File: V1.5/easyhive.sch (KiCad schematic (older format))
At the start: 105 parts, among them IC1 ATSAMD21G, IC2 BQ2407X, IC3 ADS1232, IC4 DS18B20U, IC5 XC6220B331, IC6 SARA-N310, IC7 TPS22919, J1 U.FL, J2 U.FL(2), K1 693043020611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

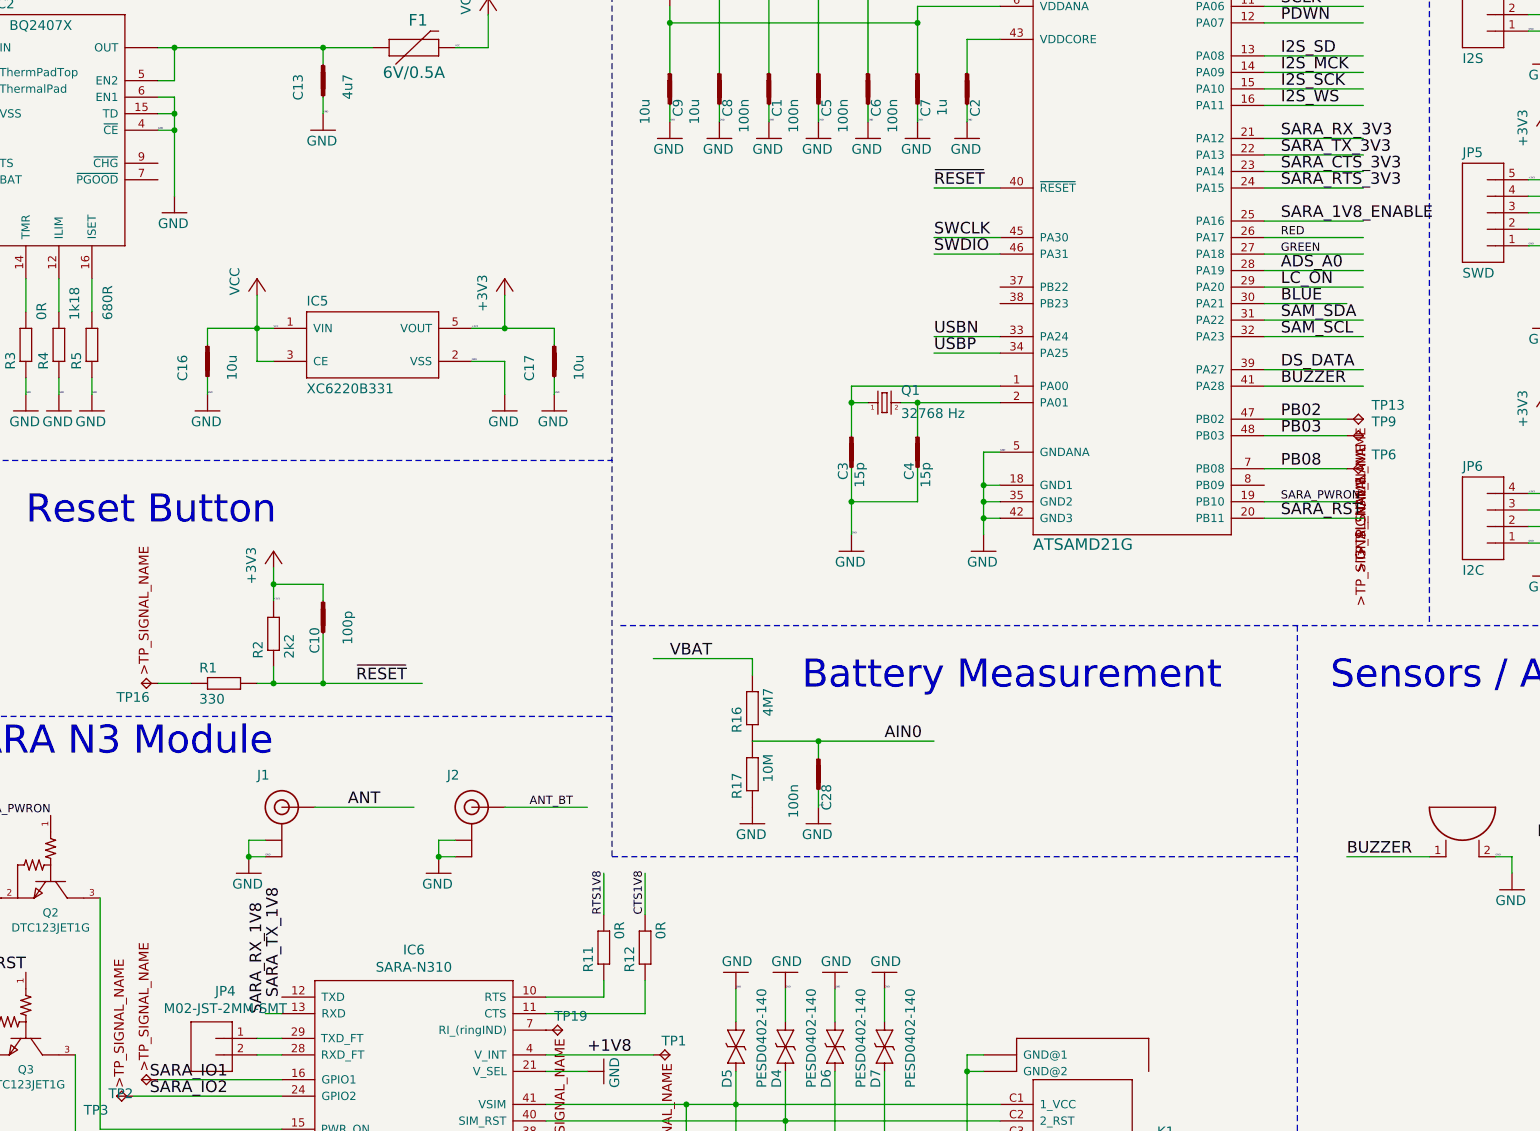
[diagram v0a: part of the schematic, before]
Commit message: Hardware optimization after Prototyp
- PA12: TX 3V3
- PA13: RX 3V3
- PA14: RTS 3V3
- PA15: CTS 3V3
- insert 2x R0 between TX/RX track
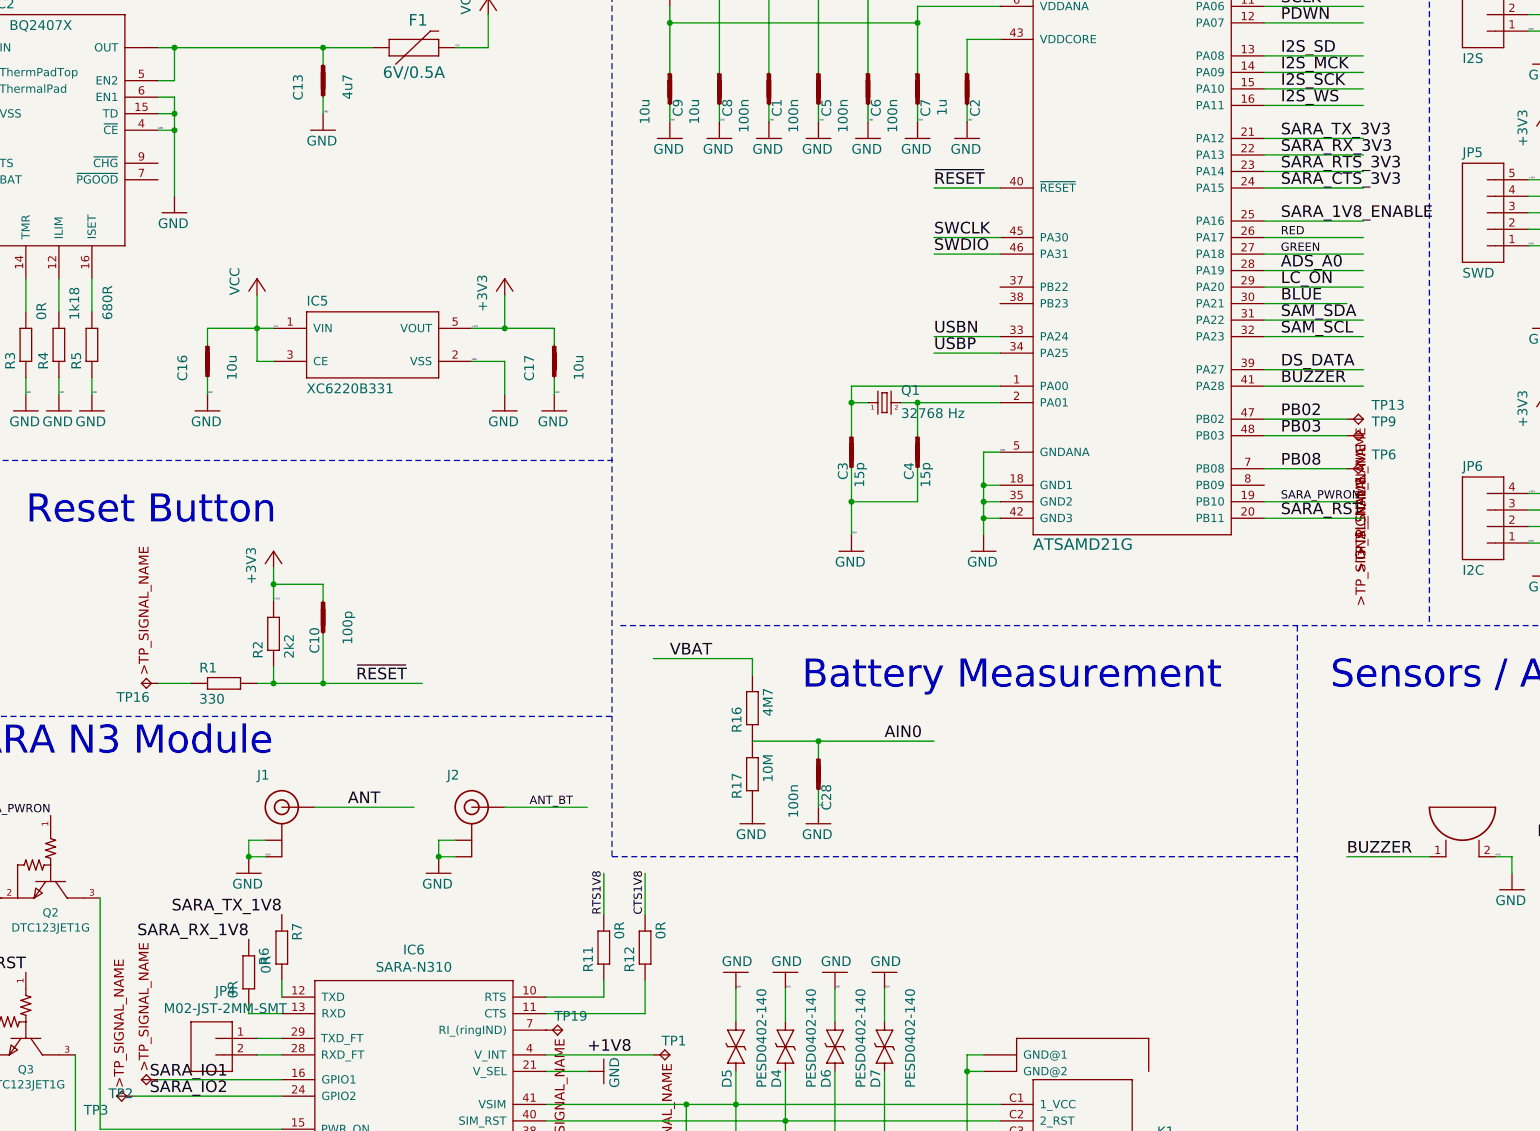
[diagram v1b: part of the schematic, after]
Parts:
- added R6, R7: 0R, easyhive:C0402, symbol easyhive:RESISTOR-0402
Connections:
- wire segments 412 -> 414
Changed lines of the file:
@@
 Text Label 12900 2250 0    70   ~ 0
 I2S_SD
-Text Label 12900 2950 0    70   ~ 0
-SARA_CTS_3V3
 Text Label 12900 3250 0    70   ~ 0
 SARA_1V8_ENABLE
-Text Label 12900 3050 0    70   ~ 0
-SARA_RTS_3V3
 Text Label 14900 7000 2    70   ~ 0
 DS_DATA
@@
 Text Label 8700 9200 0    70   ~ 0
 ANT_DET
-Text Label 6850 7950 1    70   ~ 0
-SARA_TX_1V8
-Text Label 12900 2750 0    70   ~ 0
-SARA_RX_3V3
-Text Label 6750 8050 1    70   ~ 0
-SARA_RX_1V8
-Text Label 12900 2850 0    70   ~ 0
-SARA_TX_3V3
 Text Label 6150 9650 0    70   ~ 0
 SARA_SDA
@@
 $EndComp
 $Comp
-L easyhive:MBR0520LT D1
-U 1 1 8D141E84
-P 3600 2200
-F 0 "D1" H 3700 2219 59  0000 L BNN
-F 1 "MBR0520LT" H 3700 2109 59  0000 L BNN
-F 2 "easyhive:SOD123" H 3600 2200 50  0001 C CNN
-F 3 "" H 3600 2200 50  0001 C CNN
-F 4 "auch anderer Hersteller moeglich" H 3600 2200 50  0001 C CNN "Description"
-F 5 "MBR0520LT" H 3600 2200 50  0001 C CNN "MPN"
-F 6 "ON Semiconductor" H 3600 2200 50  0001 C CNN "Manufacturer"
-	1    3600 2200
-	1    0    0    -1
-$EndComp
-$Comp
-L easyhive:MBR0520LT D2
-U 1 1 20478EC3
-P 3600 2900
-F 0 "D2" H 3700 2919 59  0000 L BNN
-F 1 "MBR0520LT" H 3700 2809 59  0000 L BNN
-F 2 "easyhive:SOD123" H 3600 2900 50  0001 C CNN
-F 3 "" H 3600 2900 50  0001 C CNN
-F 4 "auch anderer Hersteller moeglich" H 3600 2900 50  0001 C CNN "Description"
-F 5 "MBR0520LT" H 3600 2900 50  0001 C CNN "MPN"
-F 6 "ON Semiconductor" H 3600 2900 50  0001 C CNN "Manufacturer"
-	1    3600 2900
-	1    0    0    -1
-$EndComp
-$Comp
 L easyhive:CAPACITOR-0402 C11
 U 1 1 6062EDB6
@@
 Connection ~ 10700 2050
 Wire Wire Line
-	3700 2200 4300 2200
-Wire Wire Line
 	4300 2200 4700 2200
 Wire Wire Line
@@
 Wire Wire Line
 	4900 2200 4700 2200
-Connection ~ 4300 2200
 Connection ~ 4700 2200
 Wire Wire Line
-	3200 2200 3500 2200
-Wire Wire Line
 	4500 1500 4500 3000
 Wire Wire Line
@@
 $EndComp
 Wire Wire Line
-	6850 8050 6750 8050
-Wire Wire Line
 	6700 8200 6850 8200
 Wire Wire Line
 	6700 8300 6850 8300
+$Comp
+L easyhive:RESISTOR-0402 R7
+U 1 1 6035F871
+P 6850 7650
+F 0 "R7" H 6700 7709 59  0000 L BNN
+F 1 "0R" H 6900 7520 59  0000 L BNN
+F 2 "easyhive:C0402" H 6850 7650 50  0001 C CNN
+F 3 "" H 6850 7650 50  0001 C CNN
+	1    6850 7650
+	0    1    1    0
+$EndComp
+Connection ~ 4300 2200
+Wire Wire Line
+	3700 2200 4300 2200
+Wire Wire Line
+	3200 2200 3500 2200
+Wire Wire Line
+	6850 7850 6850 7950
+Wire Wire Line
+	6650 8050 6850 8050
+$Comp
+L easyhive:RESISTOR-0402 R6
+U 1 1 60361375
+P 6650 7800
+F 0 "R6" H 6500 7859 59  0000 L BNN
+F 1 "0R" H 6700 7670 59  0000 L BNN
+F 2 "easyhive:C0402" H 6650 7800 50  0001 C CNN
+F 3 "" H 6650 7800 50  0001 C CNN
+	1    6650 7800
+	0    1    1    0
+$EndComp
+Wire Wire Line
+	6650 8000 6650 8050
+Text Label 6850 7450 2    70   ~ 0
+SARA_TX_1V8
+Text Label 6650 7600 2    70   ~ 0
+SARA_RX_1V8
+Text Label 12900 2750 0    70   ~ 0
+SARA_TX_3V3
+Text Label 12900 2850 0    70   ~ 0
+SARA_RX_3V3
+Text Label 12900 2950 0    70   ~ 0
+SARA_RTS_3V3
+Text Label 12900 3050 0    70   ~ 0
+SARA_CTS_3V3
+$Comp
+L easyhive:MBR0520LT D2
+U 1 1 20478EC3
+P 3600 2900
+F 0 "D2" H 3700 2919 59  0000 L BNN
+F 1 "MBR0520LT" H 3700 2809 59  0000 L BNN
+F 2 "easyhive:SOD123" H 3600 2900 50  0001 C CNN
+F 3 "" H 3600 2900 50  0001 C CNN
+F 4 "auch anderer Hersteller moeglich" H 3600 2900 50  0001 C CNN "Description"
+F 5 "MBR0520LT" H 3600 2900 50  0001 C CNN "MPN"
+F 6 "ON Semiconductor" H 3600 2900 50  0001 C CNN "Manufacturer"
+	1    3600 2900
+	1    0    0    -1
+$EndComp
+$Comp
+L easyhive:MBR0520LT D1
+U 1 1 8D141E84
+P 3600 2200
+F 0 "D1" H 3700 2219 59  0000 L BNN
+F 1 "MBR0520LT" H 3700 2109 59  0000 L BNN
+F 2 "easyhive:SOD123" H 3600 2200 50  0001 C CNN
+F 3 "" H 3600 2200 50  0001 C CNN
+F 4 "auch anderer Hersteller moeglich" H 3600 2200 50  0001 C CNN "Description"
+F 5 "MBR0520LT" H 3600 2200 50  0001 C CNN "MPN"
+F 6 "ON Semiconductor" H 3600 2200 50  0001 C CNN "Manufacturer"
+	1    3600 2200
+	1    0    0    -1
+$EndComp
 $EndSCHEMATC
